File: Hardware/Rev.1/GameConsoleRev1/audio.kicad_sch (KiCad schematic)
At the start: 22 parts, among them J3 L Channel, J4 R Channel, SW5 SW_SPDT, U10 PAM8302AAS, U11 PAM8302AAS

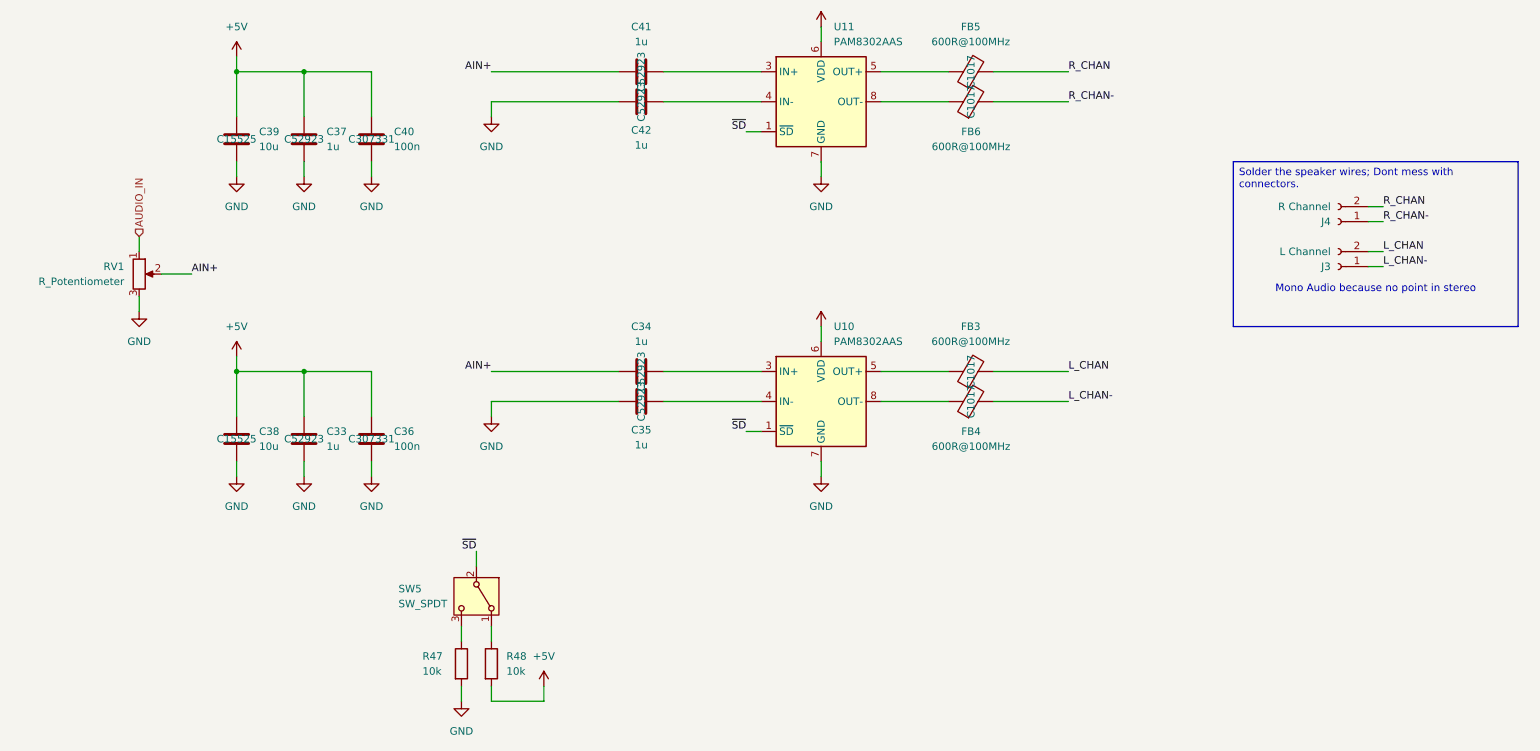
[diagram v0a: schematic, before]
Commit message: Added CPP Build
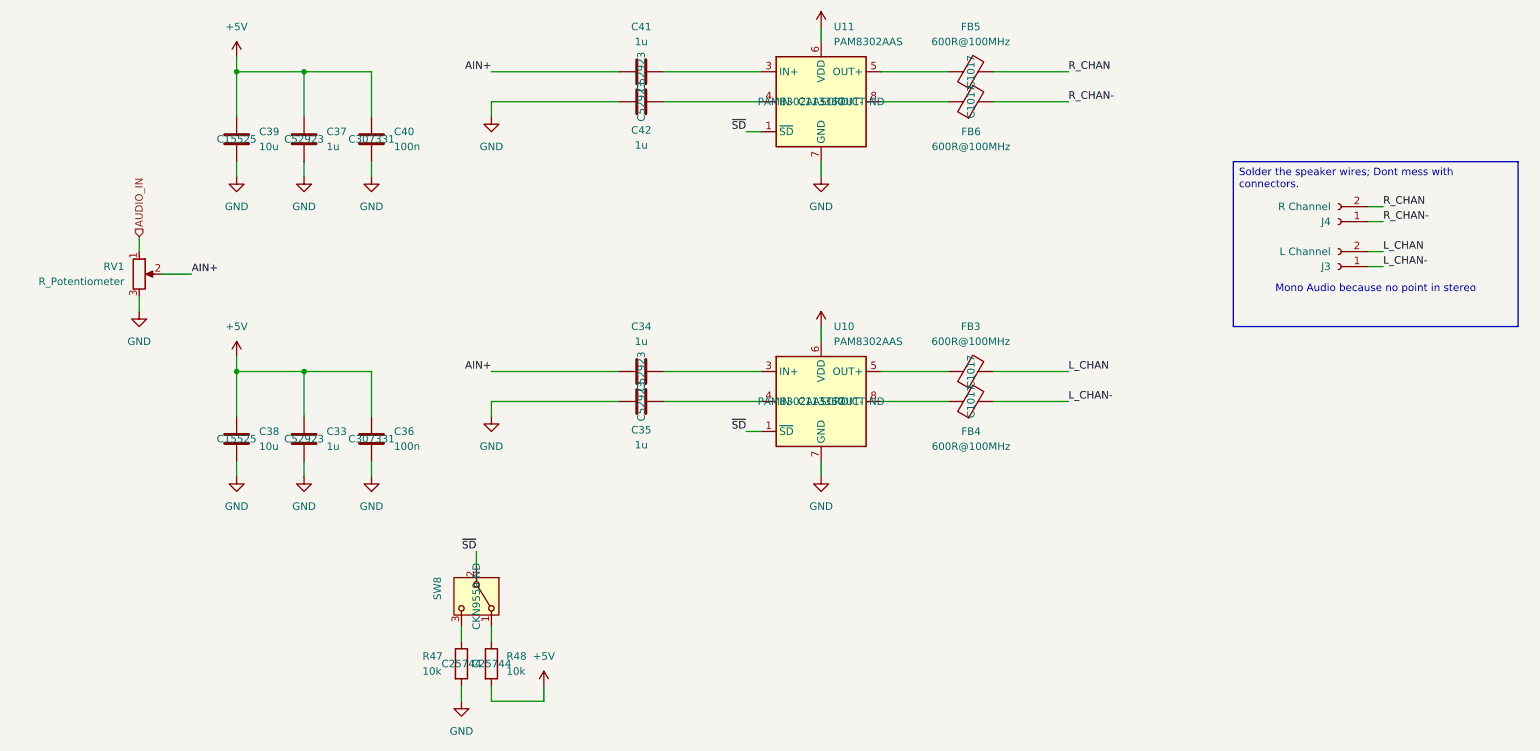
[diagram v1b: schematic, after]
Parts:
- removed SW5: SW_SPDT, Button_Switch_SMD:SW_SPDT_PCM12, symbol Switch:SW_SPDT
- added SW8: SW_SPDT, Button_Switch_THT:SW_Slide_SPDT_Angled_CK_OS102011MA1Q, symbol Switch:SW_SPDT
- R47, R48: LCSC (none) -> C25744
- U10, U11: DK# (none) -> PAM8302AASCRDICT-ND; LCSC (none) -> C113367
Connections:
- net ~{SD}: now also SW8.2 (B)
- net at R47.1: now also SW8.3 (C)
- net at R48.1: now also SW8.1 (A)
